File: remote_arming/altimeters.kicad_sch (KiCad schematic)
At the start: 42 parts, among them J10 Drogue Pyro, J5 Bypass Mag Switches, J6 A2 Connector, J7 A1 Connector, J8 SL Data Connector, J9 Main Pyros, Q1 DMG2302UK, Q2 DMG2302UK, Q3 AOD417, Q4 AOD417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

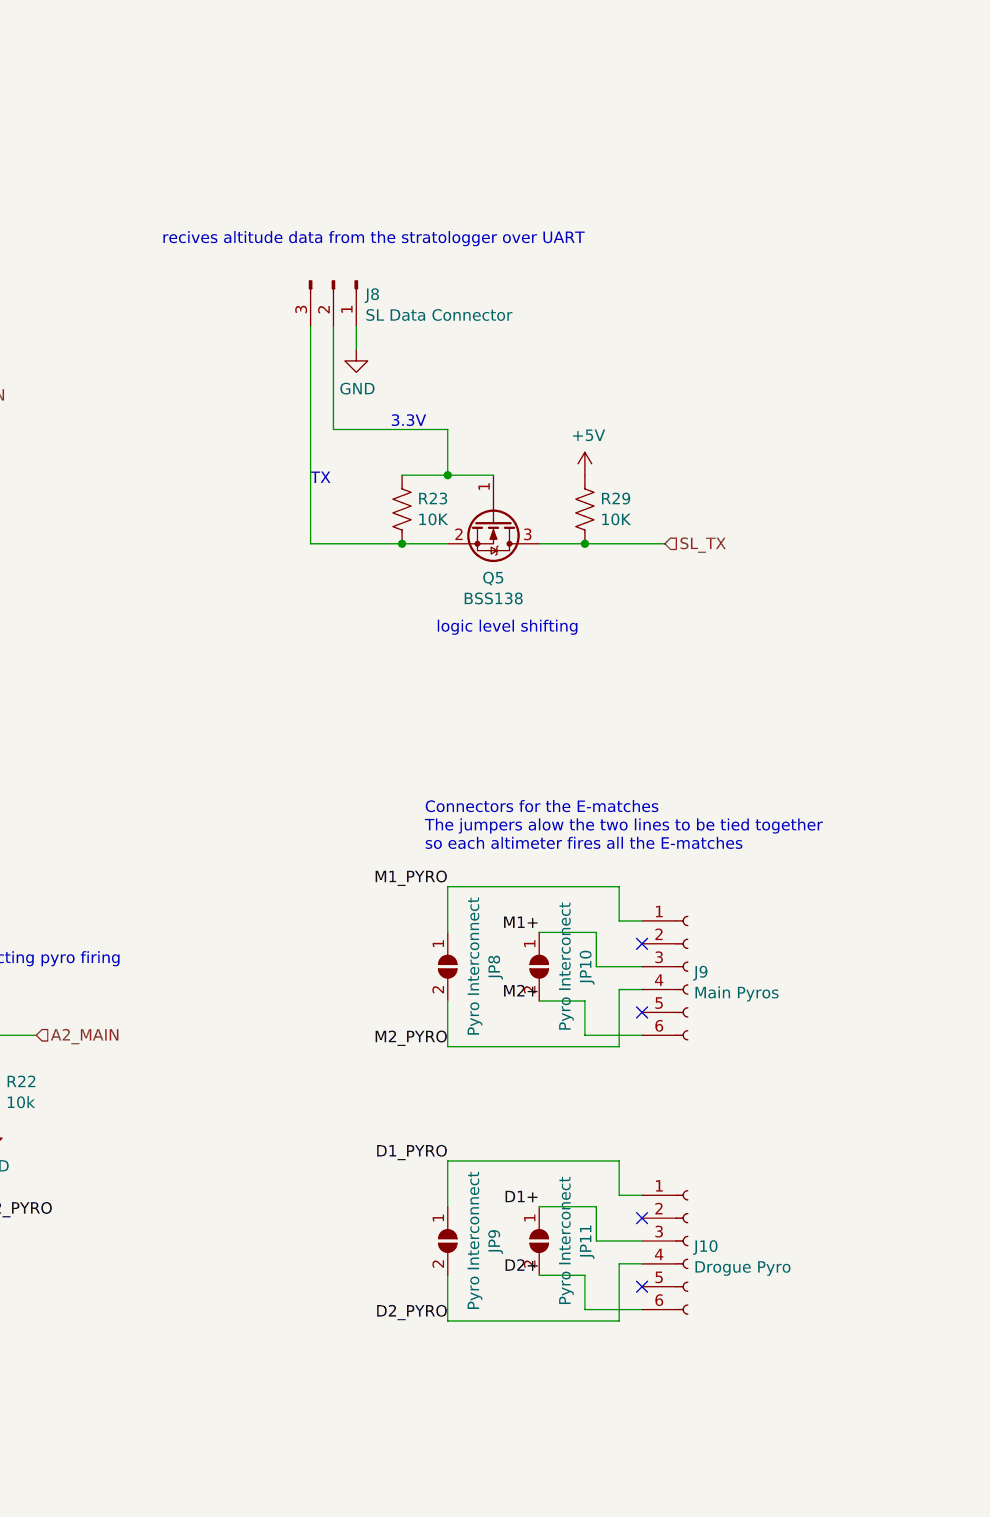
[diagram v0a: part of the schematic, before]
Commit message: removed interconnects JP8 JP9 JP10 JP11
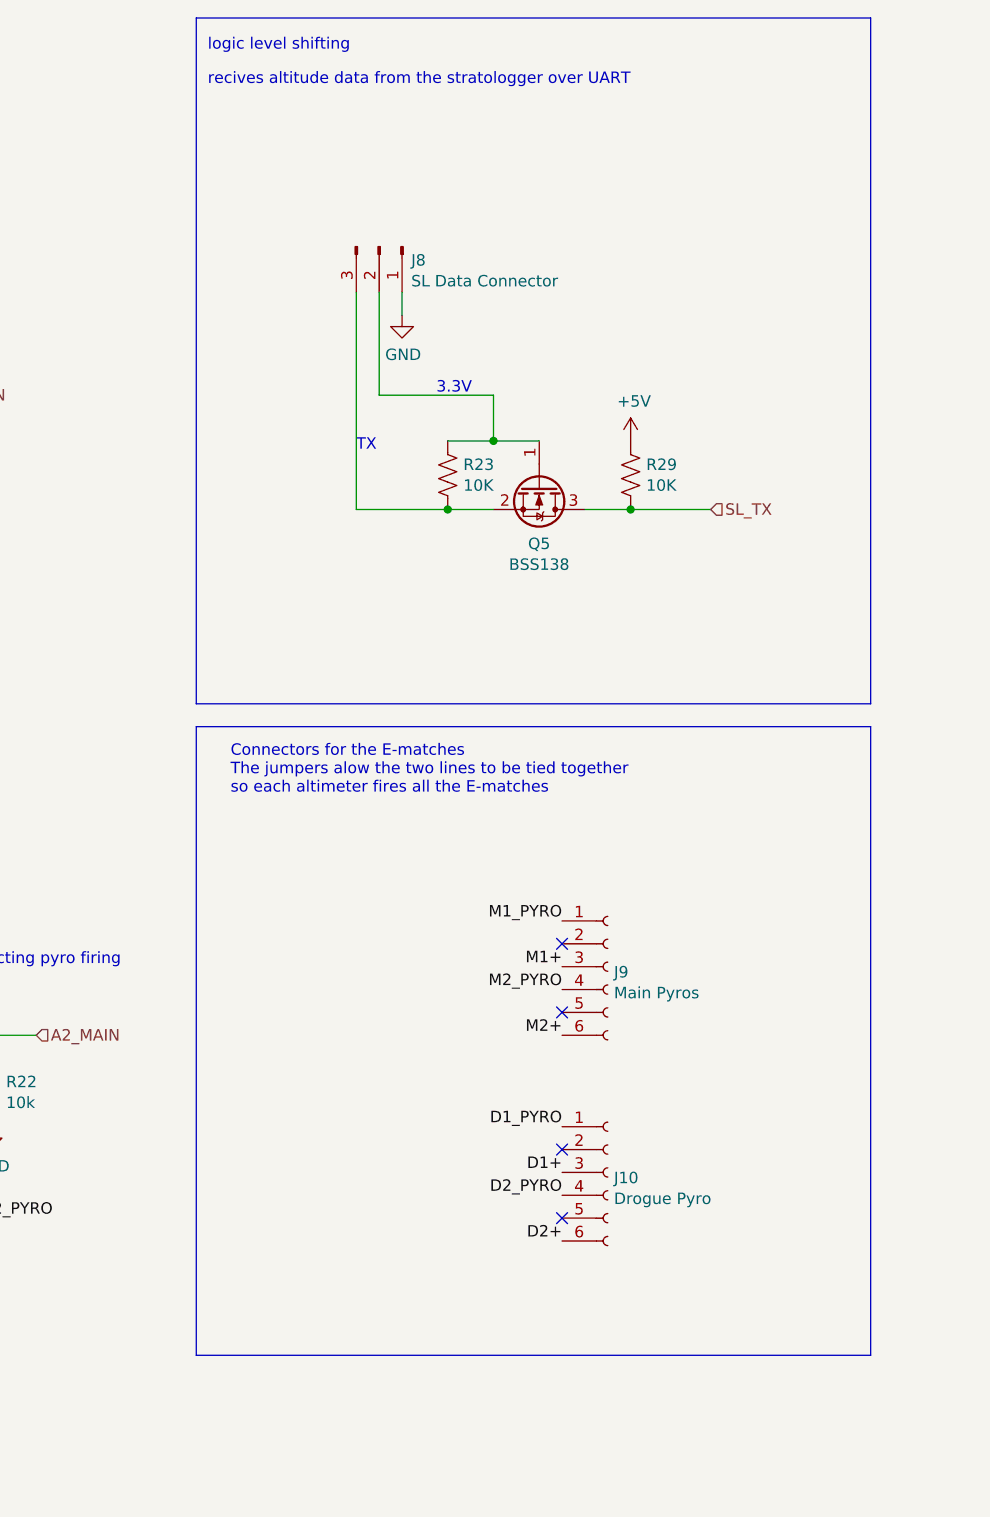
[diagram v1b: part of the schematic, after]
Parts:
- removed JP10, JP11: Pyro Interconect, Jumper:SolderJumper-2_P1.3mm_Open_RoundedPad1.0x1.5mm, symbol Jumper:SolderJumper_2_Open
- removed JP8, JP9: Pyro Interconnect, Jumper:SolderJumper-2_P1.3mm_Open_RoundedPad1.0x1.5mm, symbol Jumper:SolderJumper_2_Open
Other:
- moved on the sheet: J10, J8, J9, Q5, R23, R29

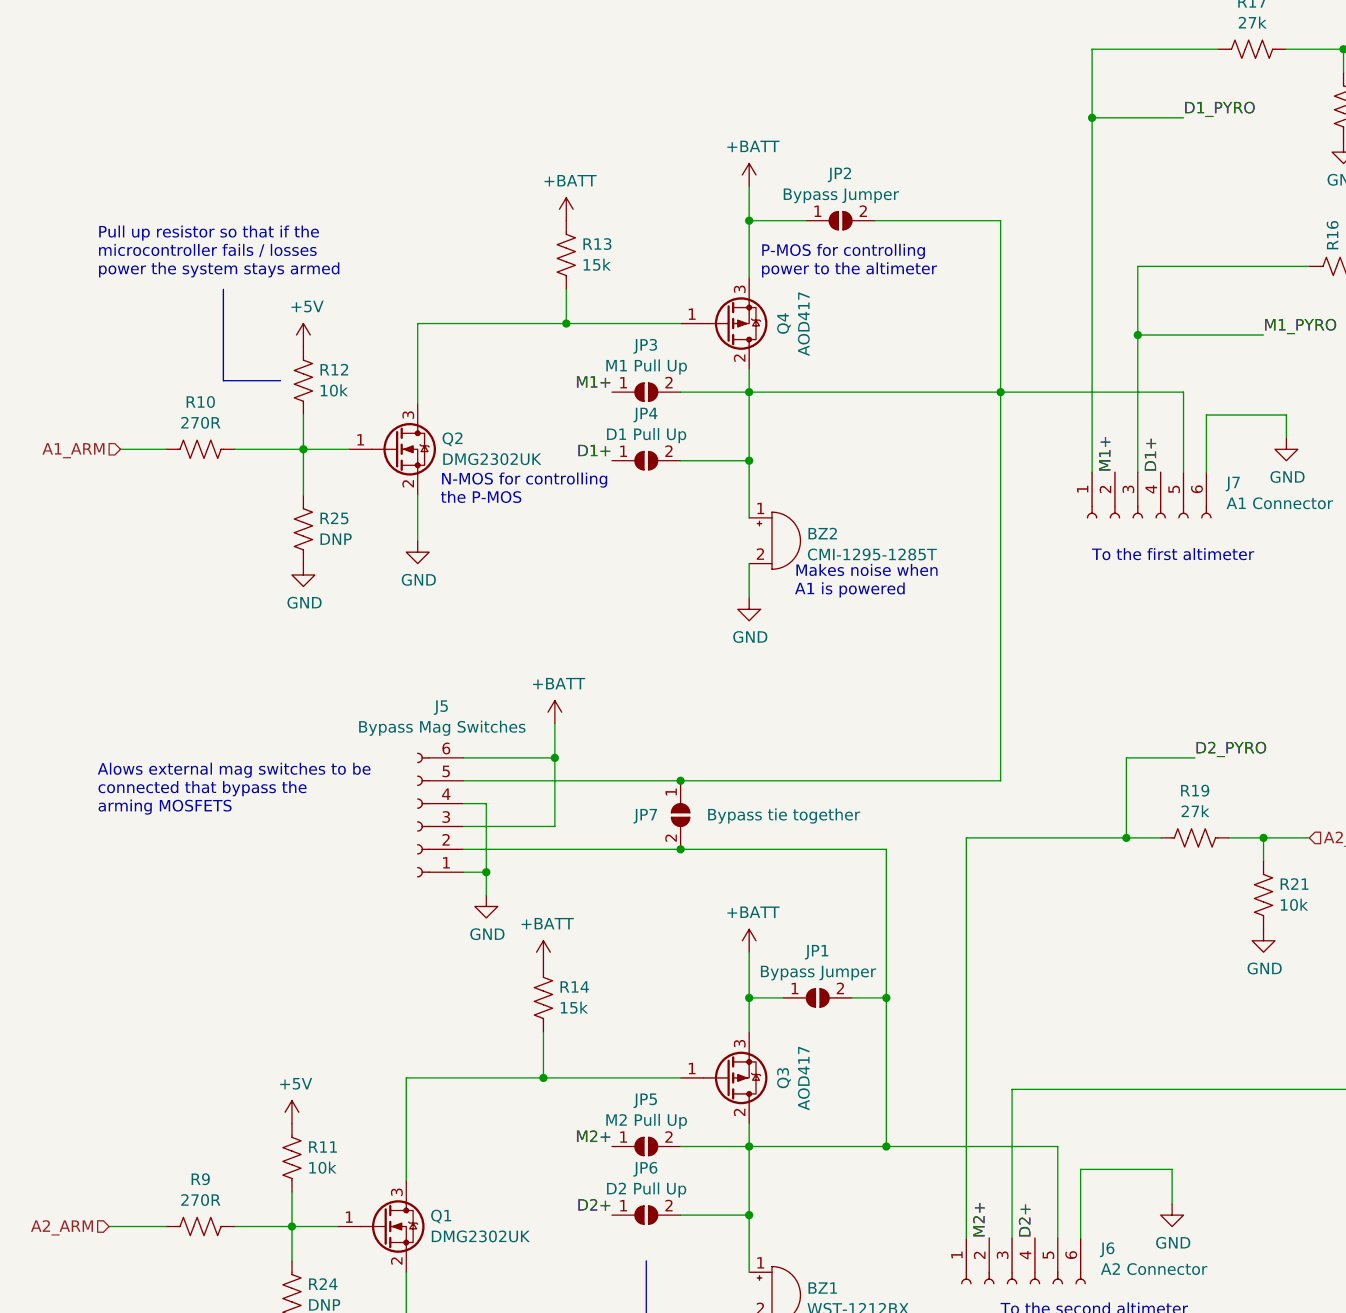
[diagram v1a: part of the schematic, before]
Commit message: removed bypass mag switches J5 and bypass jumpers JP1 JP2
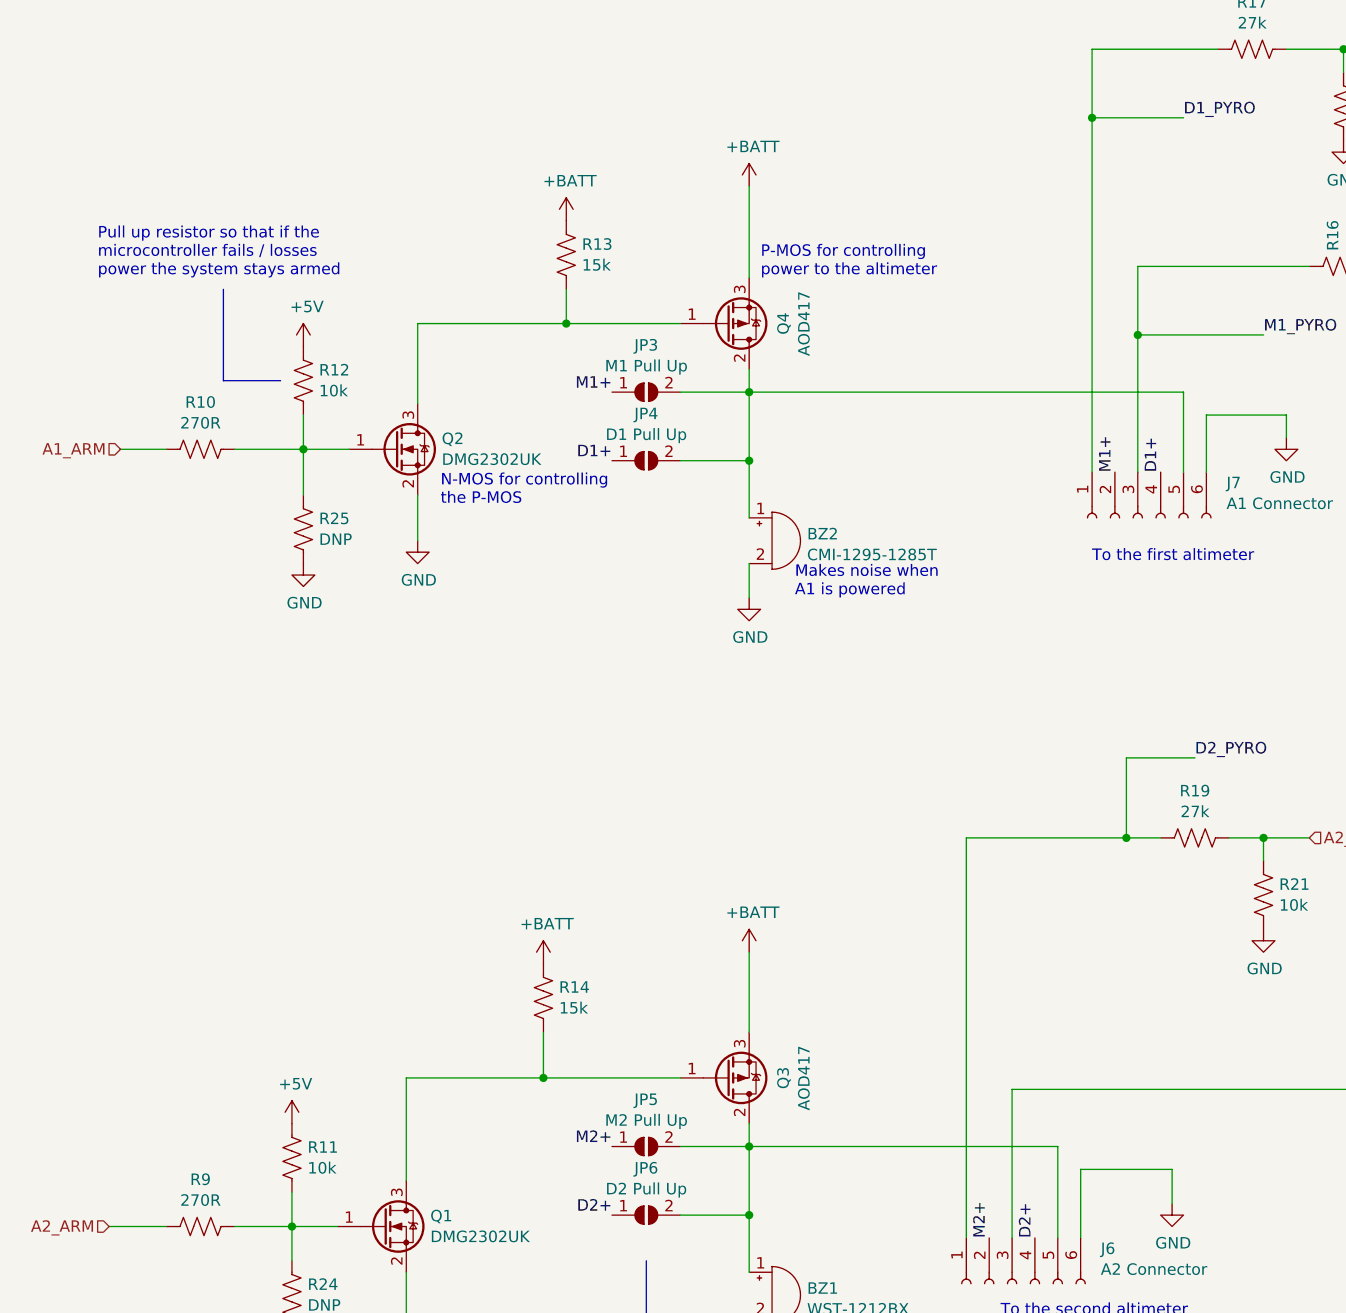
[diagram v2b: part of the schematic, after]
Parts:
- removed J5: Bypass Mag Switches, canhw_footprints:connector_Harwin_M80-5000642, symbol remote_arming-rescue:Conn_01x06_Female-Connector
- removed JP1, JP2: Bypass Jumper, Jumper:SolderJumper-2_P1.3mm_Open_RoundedPad1.0x1.5mm, symbol Jumper:SolderJumper_2_Open
- removed JP7: Bypass tie together, Jumper:SolderJumper-2_P1.3mm_Open_RoundedPad1.0x1.5mm, symbol Jumper:SolderJumper_2_Open
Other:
- note removed: "Alows external mag switches to be connected that bypass the arming MOSFETS"

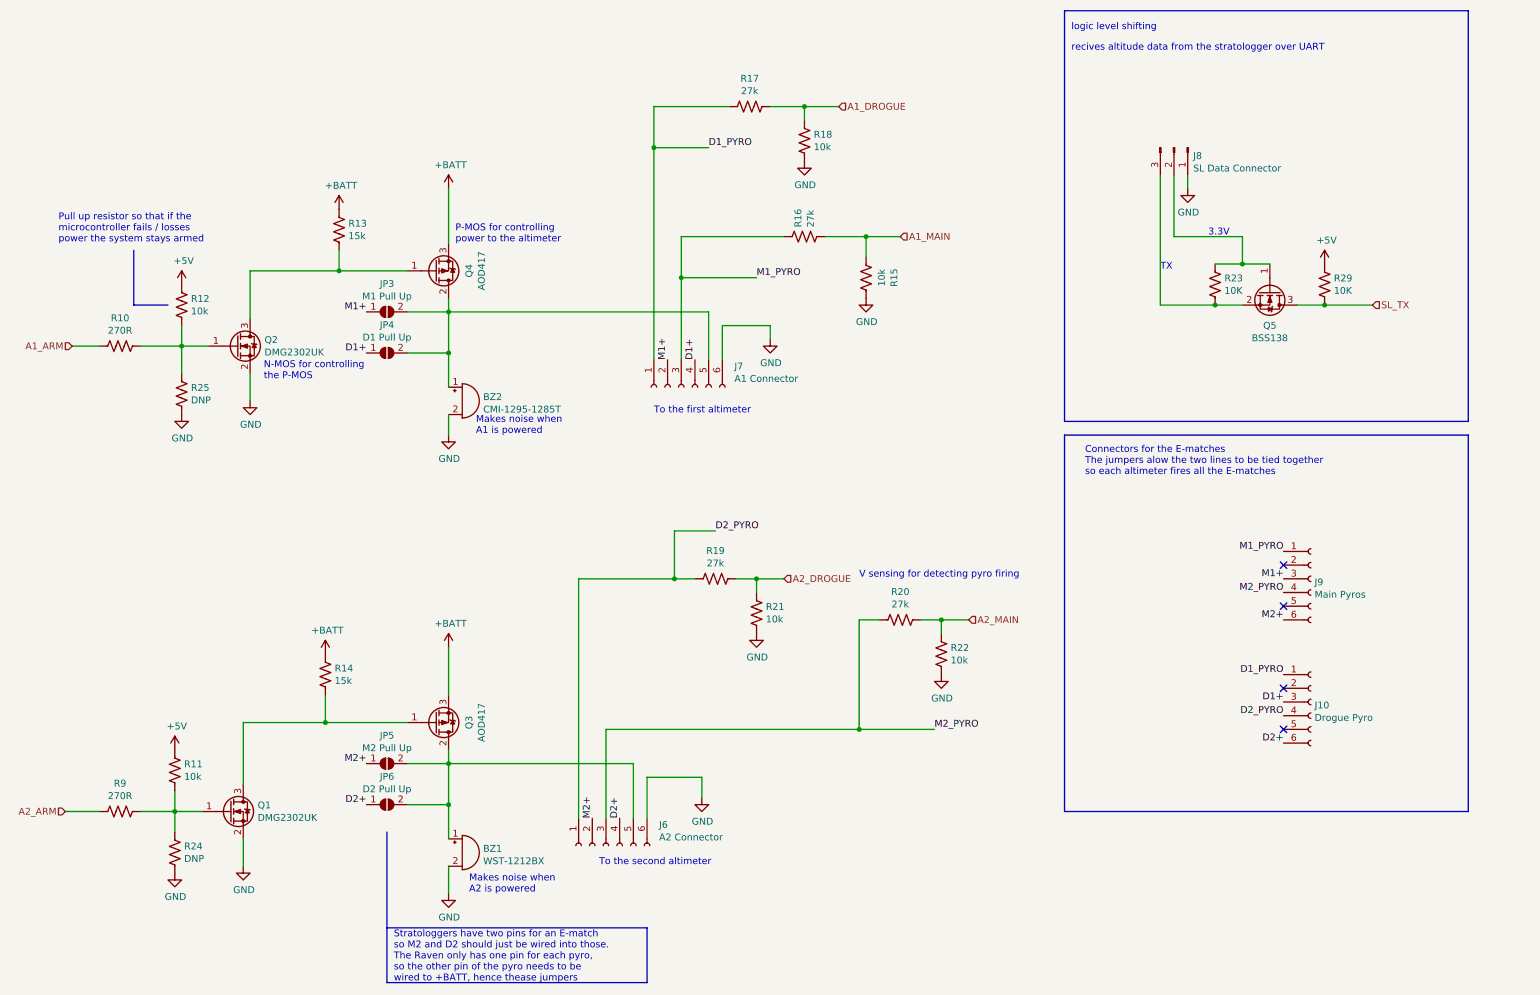
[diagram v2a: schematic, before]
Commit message: split BATT into BATT1 BATT2, LDO powered with BATT1
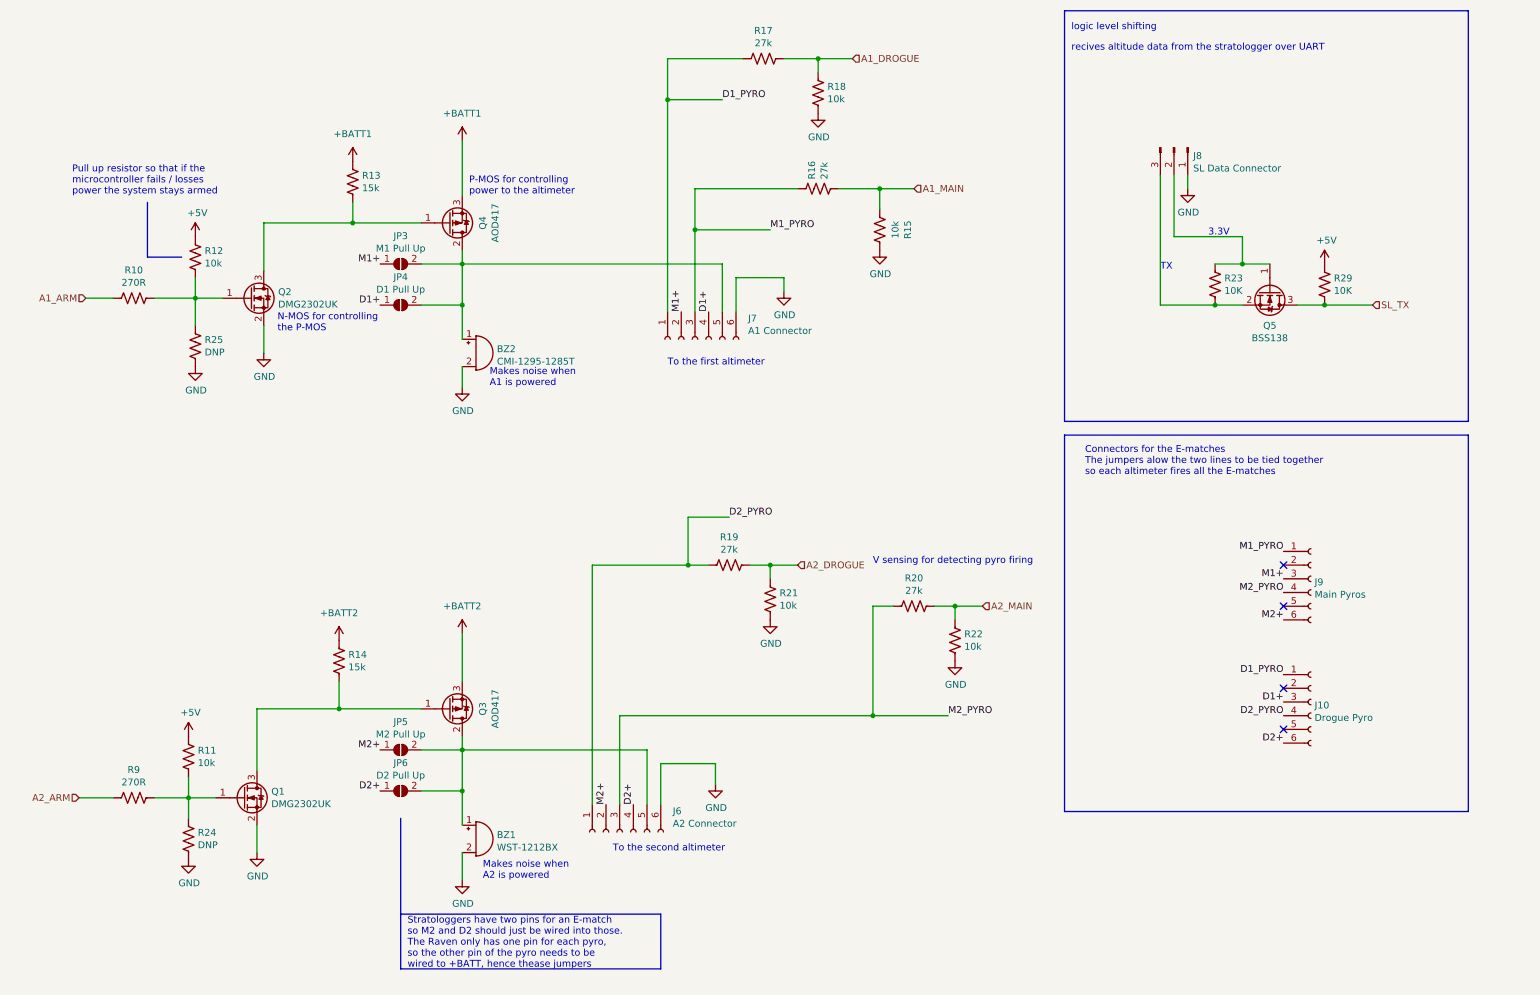
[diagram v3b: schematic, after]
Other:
- moved on the sheet: BZ1, BZ2, J6, J7, JP3, JP4, JP5, JP6, Q1, Q2, Q3, Q4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
